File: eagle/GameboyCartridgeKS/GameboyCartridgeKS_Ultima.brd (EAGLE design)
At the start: 49.3 x 58 mm, 25 parts, among them IC1 AT49F040J

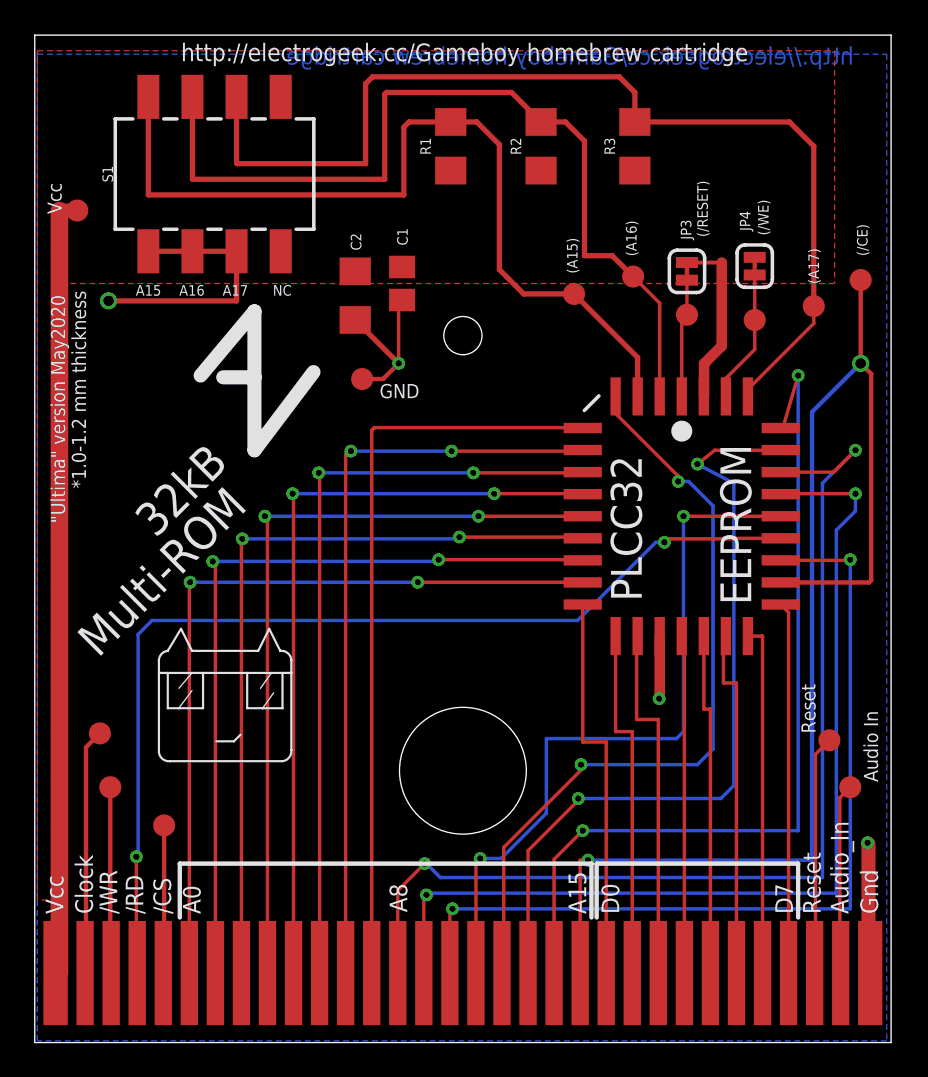
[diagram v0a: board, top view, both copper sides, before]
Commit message: Ultima GB cart looks fine and ready to prod. Will avoid to rush and post to the GB forum for feedback.
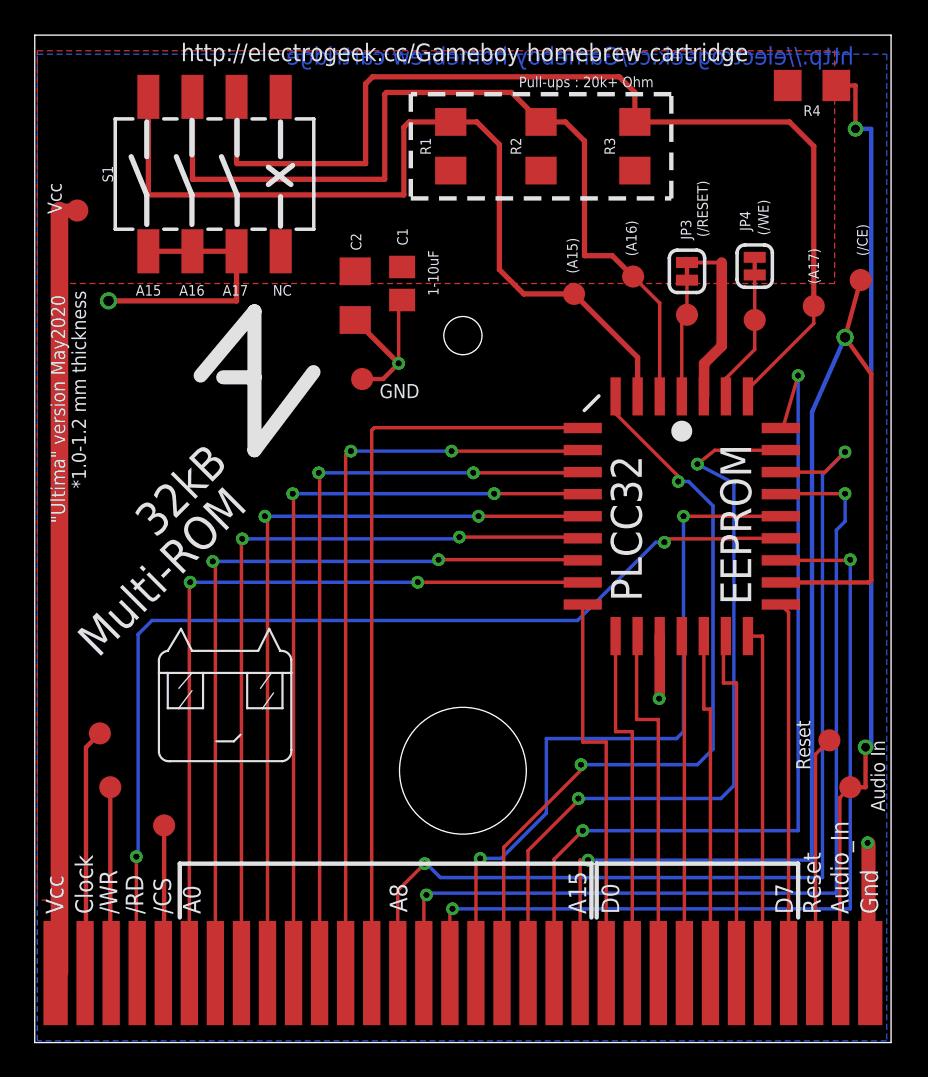
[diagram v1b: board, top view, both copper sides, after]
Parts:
- added R4: (no value), SparkFun-Resistors:1206
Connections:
- net 31: now also R4.1
- net VDD: now also R4.2
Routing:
- net 31: track 11.0 -> 54.7 mm, vias 0 -> 2
- net 21: track 72.4 -> 73.5 mm
- net 14: track 60.4 -> 59.4 mm
- net 15: track 56.0 -> 55.1 mm
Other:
- board text added: "1-10uF"
- board text added: "Pull-ups : 20k+ Ohm"
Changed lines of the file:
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@@
 <text x="20.7" y="37.1" size="0.8128" layer="21" font="vector">GND</text>
 <text x="22.3" y="7.5" size="1.016" layer="21" rot="R90">A8</text>
-<text x="45.8" y="17.8" size="0.8128" layer="21" font="vector" rot="R90">Reset</text>
-<text x="49.4" y="15" size="0.8128" layer="21" font="vector" rot="R90">Audio In</text>
+<text x="45.5" y="15.7" size="0.8128" layer="21" font="vector" rot="R90">Reset</text>
+<text x="49.8" y="13.3" size="0.8128" layer="21" font="vector" rot="R90">Audio In</text>
 <text x="35.5" y="46.3" size="0.6096" layer="21" font="vector" ratio="20" rot="R90" align="bottom-center">(A16)</text>
 <text x="46" y="44.7" size="0.6096" layer="21" font="vector" ratio="20" rot="R90" align="bottom-center">(A17)</text>
@@
 <text x="12.4" y="43" size="0.6096" layer="21" font="vector" ratio="20" align="bottom-center">A17</text>
 <text x="15.1" y="43" size="0.6096" layer="21" font="vector" ratio="20" align="bottom-center">NC</text>
+<wire x1="7.3" y1="53" x2="7.3" y2="51" width="0.3048" layer="21"/>
+<wire x1="7.3" y1="47.1" x2="7.3" y2="48.8" width="0.3048" layer="21"/>
+<wire x1="7.3" y1="48.8" x2="6.4" y2="51" width="0.3048" layer="21"/>
+<wire x1="9.9" y1="53.1" x2="9.9" y2="51.1" width="0.3048" layer="21"/>
+<wire x1="12.5" y1="53.1" x2="12.5" y2="51.1" width="0.3048" layer="21"/>
+<wire x1="9.9" y1="47.1" x2="9.9" y2="48.8" width="0.3048" layer="21"/>
+<wire x1="12.5" y1="47.1" x2="12.5" y2="48.8" width="0.3048" layer="21"/>
+<wire x1="9.9" y1="48.8" x2="9" y2="51" width="0.3048" layer="21"/>
+<wire x1="12.5" y1="48.8" x2="11.6" y2="51" width="0.3048" layer="21"/>
+<wire x1="15" y1="53" x2="15" y2="51" width="0.3048" layer="21"/>
+<wire x1="15" y1="47" x2="15" y2="48.7" width="0.3048" layer="21"/>
+<wire x1="14.3" y1="50.4" x2="15.6" y2="49.4" width="0.3048" layer="21"/>
+<wire x1="15.7" y1="50.5" x2="14.3" y2="49.4" width="0.3048" layer="21"/>
+<text x="24.1" y="44.3" size="0.6096" layer="21" font="vector" ratio="20" rot="R90" align="bottom-center">1-10uF</text>
+<wire x1="22.5" y1="54.6" x2="22.5" y2="48.6" width="0.254" layer="21" style="shortdash"/>
+<wire x1="22.5" y1="48.6" x2="37.5" y2="48.6" width="0.254" layer="21" style="shortdash"/>
+<wire x1="37.5" y1="48.6" x2="37.5" y2="54.6" width="0.254" layer="21" style="shortdash"/>
+<wire x1="37.5" y1="54.6" x2="22.5" y2="54.6" width="0.254" layer="21" style="shortdash"/>
+<text x="32.6" y="55" size="0.6096" layer="21" font="vector" ratio="20" align="bottom-center">Pull-ups : 20k+ Ohm</text>
 </plain>
 <attributes>
@@
 </element>
 <element name="TP13" library="SparkFun-Connectors" library_urn="urn:adsk.eagle:library:513" package="PAD.03X.05" package3d_urn="urn:adsk.eagle:package:38285/1" value="TEST-POINT3X5" x="48.4" y="43.9" smashed="yes"/>
+<element name="R4" library="SparkFun-Resistors" package="1206" value=" " x="45.6" y="55.1" smashed="yes" rot="R180">
+<attribute name="NAME" x="45.6" y="53.957" size="0.6096" layer="25" font="vector" ratio="20" rot="R180" align="bottom-center"/>
+<attribute name="PROD_ID" value=" " x="45.6" y="55.1" size="1.778" layer="27" rot="R180" display="off"/>
+<attribute name="VALUE" x="45.6" y="56.243" size="0.6096" layer="27" font="vector" ratio="20" rot="R180" align="top-center"/>
+</element>
 </elements>
 <signals>
@@
 <contactref element="R2" pad="1"/>
 <contactref element="R1" pad="1"/>
+<contactref element="R4" pad="2"/>
 <wire x1="2.2724" y1="4" x2="2.05" y2="4" width="0" layer="19" extent="1-1"/>
 </signal>
@@
 <via x="32.7" y="10.5" extent="1-16" drill="0.35"/>
 <wire x1="32.7" y1="10.5" x2="45.6" y2="10.5" width="0.2" layer="16"/>
-<wire x1="48.4" y1="39.1" x2="45.6" y2="36.3" width="0.254" layer="16"/>
+<wire x1="47.5" y1="40.6" x2="45.6" y2="36.3" width="0.254" layer="16"/>
 <wire x1="45.6" y1="36.3" x2="45.6" y2="10.5" width="0.254" layer="16"/>
-<via x="48.4" y="39.1" extent="1-16" drill="0.6" shape="square"/>
+<via x="47.5" y="40.6" extent="1-16" drill="0.6" shape="square"/>
 <contactref element="IC1" pad="22"/>
 <contactref element="TP13" pad="P$1"/>
-<wire x1="48.4" y1="39.1" x2="49.007" y2="38.493" width="0.254" layer="1"/>
+<wire x1="47.5" y1="40.6" x2="49.007" y2="38.493" width="0.254" layer="1"/>
 <wire x1="48.89" y1="26.49" x2="43.8" y2="26.49" width="0.254" layer="1"/>
 <wire x1="49.007" y1="38.493" x2="49.007" y2="26.607" width="0.254" layer="1"/>
 <wire x1="49.007" y1="26.607" x2="48.89" y2="26.49" width="0.254" layer="1"/>
-<wire x1="48.4" y1="43.9" x2="48.4" y2="39.1" width="0.254" layer="1"/>
+<wire x1="48.4" y1="43.9" x2="47.5" y2="40.6" width="0.254" layer="1"/>
 </signal>
 <signal name="20">
@@
 <wire x1="23.4" y1="10.3" x2="24.2" y2="9.5" width="0.2" layer="16"/>
 <wire x1="24.2" y1="9.5" x2="46.2" y2="9.5" width="0.2" layer="16"/>
-<wire x1="46.2" y1="32.2" x2="48.1" y2="34.1" width="0.2" layer="16"/>
-<via x="48.1" y="34.1" extent="1-16" drill="0.35"/>
-<wire x1="48.1" y1="34.1" x2="46.84" y2="32.84" width="0.2" layer="1"/>
-<wire x1="46.84" y1="32.84" x2="43.8" y2="32.84" width="0.2" layer="1"/>
-<wire x1="46.2" y1="9.5" x2="46.2" y2="32.2" width="0.2" layer="16"/>
+<wire x1="46.2" y1="32.7" x2="47.5" y2="34" width="0.2" layer="16"/>
+<via x="47.5" y="34" extent="1-16" drill="0.35"/>
+<wire x1="47.5" y1="34" x2="46.34" y2="32.84" width="0.2" layer="1"/>
+<wire x1="46.34" y1="32.84" x2="43.8" y2="32.84" width="0.2" layer="1"/>
+<wire x1="46.2" y1="9.5" x2="46.2" y2="32.7" width="0.2" layer="16"/>
 </signal>
 <signal name="15">
@@
 <wire x1="23.4" y1="8.5" x2="23.5" y2="8.6" width="0.2" layer="16"/>
 <wire x1="23.5" y1="8.6" x2="47" y2="8.6" width="0.2" layer="16"/>
-<wire x1="47" y1="29.5" x2="48.1" y2="30.6" width="0.2" layer="16"/>
-<wire x1="48.1" y1="30.6" x2="48.1" y2="31.6" width="0.2" layer="16"/>
-<via x="48.1" y="31.6" extent="1-16" drill="0.35"/>
+<wire x1="47" y1="29.5" x2="47.5" y2="30" width="0.2" layer="16"/>
+<wire x1="47.5" y1="30" x2="47.5" y2="31.6" width="0.2" layer="16"/>
+<via x="47.5" y="31.6" extent="1-16" drill="0.35"/>
 <wire x1="43.8" y1="31.57" x2="43.83" y2="31.6" width="0.2" layer="1"/>
-<wire x1="48.1" y1="31.6" x2="43.83" y2="31.6" width="0.2" layer="1"/>
+<wire x1="47.5" y1="31.6" x2="43.83" y2="31.6" width="0.2" layer="1"/>
 <wire x1="47" y1="8.6" x2="47" y2="29.5" width="0.2" layer="16"/>
 </signal>
@@
 <wire x1="47.2" y1="14.1" x2="47.2" y2="4.05" width="0.2" layer="1"/>
 <wire x1="47.2" y1="4.05" x2="47.25" y2="4" width="0.2" layer="1"/>
+<contactref element="R4" pad="1"/>
+<wire x1="48.2" y1="14.7" x2="48" y2="14.7" width="0.254" layer="1"/>
+<wire x1="48" y1="14.7" x2="47.8" y2="14.7" width="0.254" layer="1"/>
+<wire x1="47" y1="55.1" x2="48.1" y2="55.1" width="0.254" layer="1"/>
+<wire x1="48.1" y1="55.1" x2="48.1" y2="52.6" width="0.254" layer="1"/>
+<via x="48.1" y="52.6" extent="1-16" drill="0.5" shape="square"/>
+<wire x1="48.1" y1="52.6" x2="49.007" y2="52.6" width="0.254" layer="16"/>
+<wire x1="49.007" y1="17" x2="48.6808" y2="17" width="0.254" layer="16"/>
+<via x="48.6808" y="17" extent="1-16" drill="0.5"/>
+<wire x1="48.6808" y1="17" x2="48.6808" y2="14.7" width="0.254" layer="1"/>
+<wire x1="48.6808" y1="14.7" x2="48.2" y2="14.7" width="0.254" layer="1"/>
+<wire x1="49.007" y1="52.6" x2="49.007" y2="17" width="0.254" layer="16"/>
 </signal>
 <signal name="N$1">

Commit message: Added solderpads in addition to the SMD DIL toggle switch.
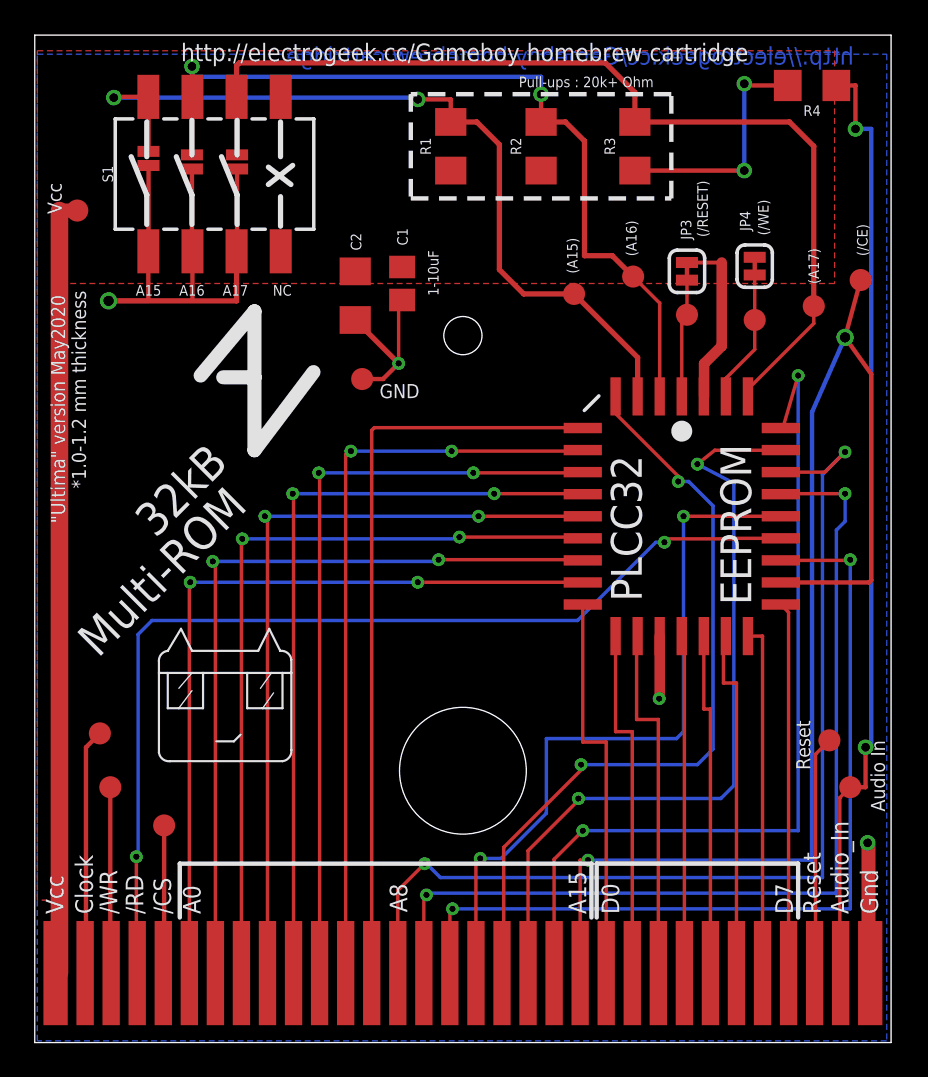
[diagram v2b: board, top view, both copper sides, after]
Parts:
- added JP1, JP2, JP5: JUMPER-SMT_2_NO_NO-SILK, SparkFun-Jumpers:SMT-JUMPER_2_NO_NO-SILK
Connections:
- net GND: now also JP1.2, JP2.2, JP5.2
- net N$4: now also JP1.1
- net N$8: now also JP2.1
- net N$9: now also JP5.1
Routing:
- net GND: track 36.9 -> 59.7 mm
- net VDD: track 57.4 -> 71.9 mm, vias 0 -> 2
- net N$9: track 60.5 -> 57.5 mm
- net N$8: track 51.0 -> 49.0 mm, vias 0 -> 2
- net N$4: track 49.9 -> 48.8 mm, vias 0 -> 2
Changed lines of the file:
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@@
 <attribute name="VALUE" x="45.6" y="56.243" size="0.6096" layer="27" font="vector" ratio="20" rot="R180" align="top-center"/>
+</element>
+<element name="JP1" library="SparkFun-Jumpers" package="SMT-JUMPER_2_NO_NO-SILK" package3d_urn="urn:adsk.eagle:package:39277/1" value="JUMPER-SMT_2_NO_NO-SILK" x="7.4" y="50.9" smashed="yes" rot="R270">
+<attribute name="VALUE" x="6.257" y="50.9" size="0.6096" layer="27" font="vector" ratio="20" rot="R270" align="top-center"/>
+</element>
+<element name="JP2" library="SparkFun-Jumpers" package="SMT-JUMPER_2_NO_NO-SILK" package3d_urn="urn:adsk.eagle:package:39277/1" value="JUMPER-SMT_2_NO_NO-SILK" x="9.9" y="50.7" smashed="yes" rot="R270">
+<attribute name="VALUE" x="8.757" y="50.7" size="0.6096" layer="27" font="vector" ratio="20" rot="R270" align="top-center"/>
+</element>
+<element name="JP5" library="SparkFun-Jumpers" package="SMT-JUMPER_2_NO_NO-SILK" package3d_urn="urn:adsk.eagle:package:39277/1" value="JUMPER-SMT_2_NO_NO-SILK" x="12.5" y="50.7" smashed="yes" rot="R270">
+<attribute name="VALUE" x="11.357" y="50.7" size="0.6096" layer="27" font="vector" ratio="20" rot="R270" align="top-center"/>
 </element>
 </elements>
@@
 <wire x1="48.95" y1="4" x2="48.85" y2="4.1" width="0.2" layer="1"/>
 <wire x1="48.85" y1="11.45" x2="48.85" y2="4.1" width="0.8128" layer="1"/>
-<via x="48.8" y="11.5" extent="1-16" drill="0.35"/>
+<via x="48.8" y="11.5" extent="1-16" drill="0.5"/>
 <wire x1="48.8" y1="11.5" x2="48.7" y2="11.6" width="0.2" layer="16"/>
 <via x="21.8" y="39.1" extent="1-16" drill="0.35"/>
@@
 <contactref element="S1" pad="7"/>
 <contactref element="S1" pad="8"/>
-<wire x1="7.39" y1="45.555" x2="9.93" y2="45.555" width="0.3048" layer="1"/>
-<wire x1="9.93" y1="45.555" x2="12.47" y2="45.555" width="0.3048" layer="1"/>
+<wire x1="12.3" y1="45.555" x2="12.47" y2="45.555" width="0.3048" layer="1"/>
 <wire x1="12.47" y1="45.555" x2="12.47" y2="42.7" width="0.3048" layer="1"/>
 <wire x1="12.47" y1="42.7" x2="5.1" y2="42.7" width="0.3048" layer="1"/>
 <via x="5.1" y="42.7" extent="1-16" drill="0.6" shape="square"/>
+<contactref element="JP1" pad="2"/>
+<contactref element="JP2" pad="2"/>
+<contactref element="JP5" pad="2"/>
+<wire x1="7.4" y1="50.2936" x2="7.4" y2="50.4936" width="0.254" layer="1"/>
+<wire x1="9.9" y1="50.2936" x2="9.9" y2="45.555" width="0.254" layer="1"/>
+<wire x1="9.9" y1="45.555" x2="9.93" y2="45.555" width="0.254" layer="1"/>
+<wire x1="12.5" y1="50.2936" x2="12.5" y2="45.555" width="0.254" layer="1"/>
+<wire x1="12.5" y1="45.555" x2="12.3" y2="45.555" width="0.254" layer="1"/>
+<wire x1="7.4" y1="50.4936" x2="7.4" y2="45.555" width="0.254" layer="1"/>
+<wire x1="7.4" y1="45.555" x2="7.39" y2="45.555" width="0.254" layer="1"/>
+<wire x1="7.39" y1="45.555" x2="7.39" y2="42.7" width="0.254" layer="1"/>
+<wire x1="7.39" y1="42.7" x2="5.1" y2="42.7" width="0.254" layer="1"/>
+<wire x1="9.93" y1="45.555" x2="9.93" y2="42.7" width="0.254" layer="1"/>
+<wire x1="9.93" y1="42.7" x2="5.1" y2="42.7" width="0.254" layer="1"/>
 </signal>
 <signal name="VDD">
@@
 <contactref element="R1" pad="1"/>
 <contactref element="R4" pad="2"/>
+<wire x1="44.2" y1="55.1" x2="41.4" y2="55.1" width="0.254" layer="1"/>
+<wire x1="41.4" y1="55.1" x2="41.4" y2="55.2" width="0.254" layer="1"/>
+<wire x1="41.4" y1="55.2" x2="41.7" y2="55.2" width="0.254" layer="1"/>
+<via x="41.7" y="55.2" extent="1-16" drill="0.5"/>
+<wire x1="41.7" y1="55.2" x2="41.7" y2="50.2" width="0.254" layer="16"/>
+<via x="41.7" y="50.2" extent="1-16" drill="0.5"/>
+<wire x1="41.7" y1="50.2" x2="35.4" y2="50.2" width="0.254" layer="1"/>
 <wire x1="2.2724" y1="4" x2="2.05" y2="4" width="0" layer="19" extent="1-1"/>
 </signal>
@@
 <contactref element="IC1" pad="3"/>
 <contactref element="TP12" pad="P$1"/>
-<wire x1="24.8" y1="53" x2="22.4" y2="53" width="0.3048" layer="1"/>
-<wire x1="22.1" y1="52.7" x2="22.1" y2="48.8" width="0.3048" layer="1"/>
-<wire x1="22.1" y1="48.8" x2="7.39" y2="48.8" width="0.3048" layer="1"/>
-<wire x1="7.39" y1="48.8" x2="7.39" y2="54.445" width="0.3048" layer="1"/>
-<wire x1="22.4" y1="53" x2="22.1" y2="52.7" width="0.3048" layer="1"/>
 <wire x1="31.9" y1="43.1" x2="35.56" y2="39.44" width="0.3048" layer="1"/>
 <wire x1="35.56" y1="39.44" x2="35.56" y2="37.2" width="0.3048" layer="1"/>
@@
 <wire x1="29" y1="43.1" x2="31.9" y2="43.1" width="0.3048" layer="1"/>
 <wire x1="26.3" y1="53" x2="27.6" y2="51.7" width="0.3048" layer="1"/>
+<contactref element="JP1" pad="1"/>
+<wire x1="7.4" y1="51.3064" x2="7.4" y2="54.445" width="0.254" layer="1"/>
+<wire x1="7.4" y1="54.445" x2="7.39" y2="54.445" width="0.254" layer="1"/>
+<wire x1="7.39" y1="54.445" x2="5.4" y2="54.445" width="0.254" layer="1"/>
+<wire x1="5.4" y1="54.445" x2="5.4" y2="54.4" width="0.254" layer="1"/>
+<via x="5.4" y="54.4" extent="1-16" drill="0.5"/>
+<wire x1="5.4" y1="54.4" x2="22.9" y2="54.4" width="0.254" layer="16"/>
+<wire x1="22.9" y1="54.4" x2="22.9" y2="54.3" width="0.254" layer="16"/>
+<via x="22.9" y="54.3" extent="1-16" drill="0.5"/>
+<wire x1="22.9" y1="54.3" x2="24.8" y2="54.3" width="0.254" layer="1"/>
+<wire x1="24.8" y1="54.3" x2="24.8" y2="53" width="0.254" layer="1"/>
 </signal>
 <signal name="N$8">
@@
 <wire x1="36.83" y1="42.57" x2="35.3" y2="44.1" width="0.2" layer="1"/>
 <wire x1="35.3" y1="44.1" x2="35.1874" y2="44.1" width="0.2" layer="1"/>
-<wire x1="30" y1="53" x2="28.3" y2="54.7" width="0.3048" layer="1"/>
-<wire x1="28.3" y1="54.7" x2="21.1" y2="54.7" width="0.3048" layer="1"/>
-<wire x1="21.1" y1="54.7" x2="21" y2="54.6" width="0.3048" layer="1"/>
-<wire x1="21" y1="54.6" x2="21" y2="49.7" width="0.3048" layer="1"/>
-<wire x1="21" y1="49.7" x2="9.93" y2="49.7" width="0.3048" layer="1"/>
-<wire x1="9.93" y1="49.7" x2="9.93" y2="54.445" width="0.3048" layer="1"/>
 <wire x1="30" y1="53" x2="31.4" y2="53" width="0.3048" layer="1"/>
 <wire x1="32.5" y1="51.9" x2="32.5" y2="45.3" width="0.3048" layer="1"/>
@@
 <wire x1="34.1" y1="45.3" x2="35.3" y2="44.1" width="0.3048" layer="1"/>
 <wire x1="31.4" y1="53" x2="32.5" y2="51.9" width="0.3048" layer="1"/>
+<contactref element="JP2" pad="1"/>
+<wire x1="9.9" y1="51.1064" x2="9.9" y2="54.445" width="0.254" layer="1"/>
+<wire x1="9.9" y1="54.445" x2="9.93" y2="54.445" width="0.254" layer="1"/>
+<wire x1="9.93" y1="54.445" x2="9.93" y2="56.2" width="0.254" layer="1"/>
+<wire x1="9.93" y1="56.2" x2="9.9" y2="56.2" width="0.254" layer="1"/>
+<via x="9.9" y="56.2" extent="1-16" drill="0.5"/>
+<wire x1="9.9" y1="56.2" x2="9.9" y2="55.6" width="0.254" layer="16"/>
+<wire x1="30" y1="55.6" x2="30" y2="54.6" width="0.254" layer="16"/>
+<via x="30" y="54.6" extent="1-16" drill="0.5"/>
+<wire x1="30" y1="54.6" x2="30" y2="53" width="0.254" layer="1"/>
+<wire x1="9.9" y1="55.6" x2="30" y2="55.6" width="0.254" layer="16"/>
 </signal>
 <signal name="N$9">
@@
 <wire x1="41.91" y1="37.61" x2="45.7" y2="41.4" width="0.2" layer="1"/>
 <wire x1="35.4" y1="53" x2="35.4" y2="54.7" width="0.3048" layer="1"/>
-<wire x1="35.4" y1="54.7" x2="34.5" y2="55.6" width="0.3048" layer="1"/>
-<wire x1="34.5" y1="55.6" x2="20.3" y2="55.6" width="0.3048" layer="1"/>
-<wire x1="20.3" y1="55.6" x2="19.9" y2="55.2" width="0.3048" layer="1"/>
-<wire x1="19.9" y1="55.2" x2="19.9" y2="50.6" width="0.3048" layer="1"/>
-<wire x1="19.9" y1="50.6" x2="12.5" y2="50.6" width="0.3048" layer="1"/>
-<wire x1="12.5" y1="50.6" x2="12.47" y2="50.63" width="0.3048" layer="1"/>
-<wire x1="12.47" y1="50.63" x2="12.47" y2="54.445" width="0.3048" layer="1"/>
+<wire x1="35.4" y1="54.7" x2="33.7" y2="56.4" width="0.3048" layer="1"/>
+<wire x1="12.47" y1="54.445" x2="12.47" y2="56.245" width="0.3048" layer="1"/>
+<wire x1="12.625" y1="56.4" x2="12.47" y2="56.245" width="0.3048" layer="1"/>
+<wire x1="33.7" y1="56.4" x2="12.625" y2="56.4" width="0.3048" layer="1"/>
 <wire x1="35.4" y1="53" x2="44.3" y2="53" width="0.3048" layer="1"/>
 <wire x1="44.3" y1="53" x2="45.7" y2="51.6" width="0.3048" layer="1"/>
 <wire x1="45.7" y1="51.6" x2="45.7" y2="42.3" width="0.3048" layer="1"/>
+<contactref element="JP5" pad="1"/>
+<wire x1="12.5" y1="51.1064" x2="12.5" y2="54.445" width="0.254" layer="1"/>
+<wire x1="12.5" y1="54.445" x2="12.47" y2="54.445" width="0.254" layer="1"/>
 </signal>
 </signals>
